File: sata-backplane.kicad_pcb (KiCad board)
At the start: 2 copper layers, 100 x 60 mm, 42 parts, among them J5 457180002, J6 G40H3132212HR

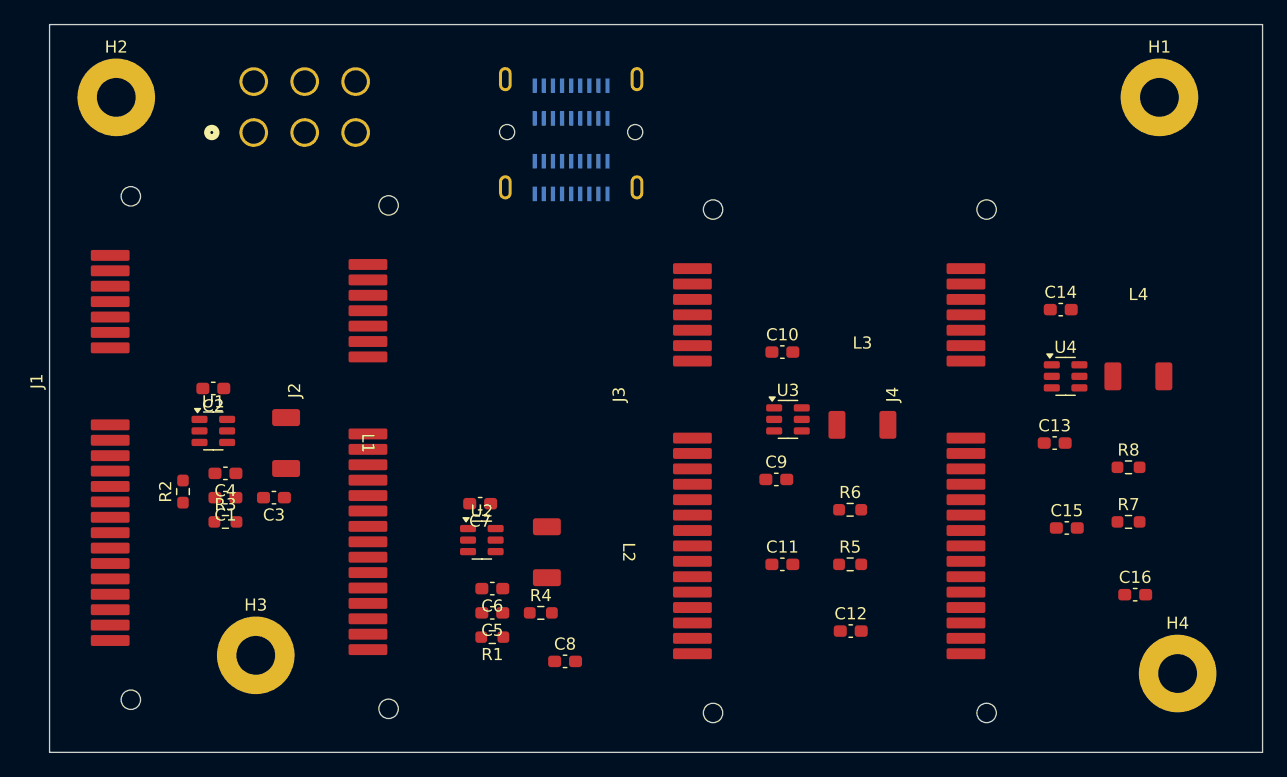
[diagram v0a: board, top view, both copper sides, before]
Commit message: Switch to two 3A converters from 4 2A
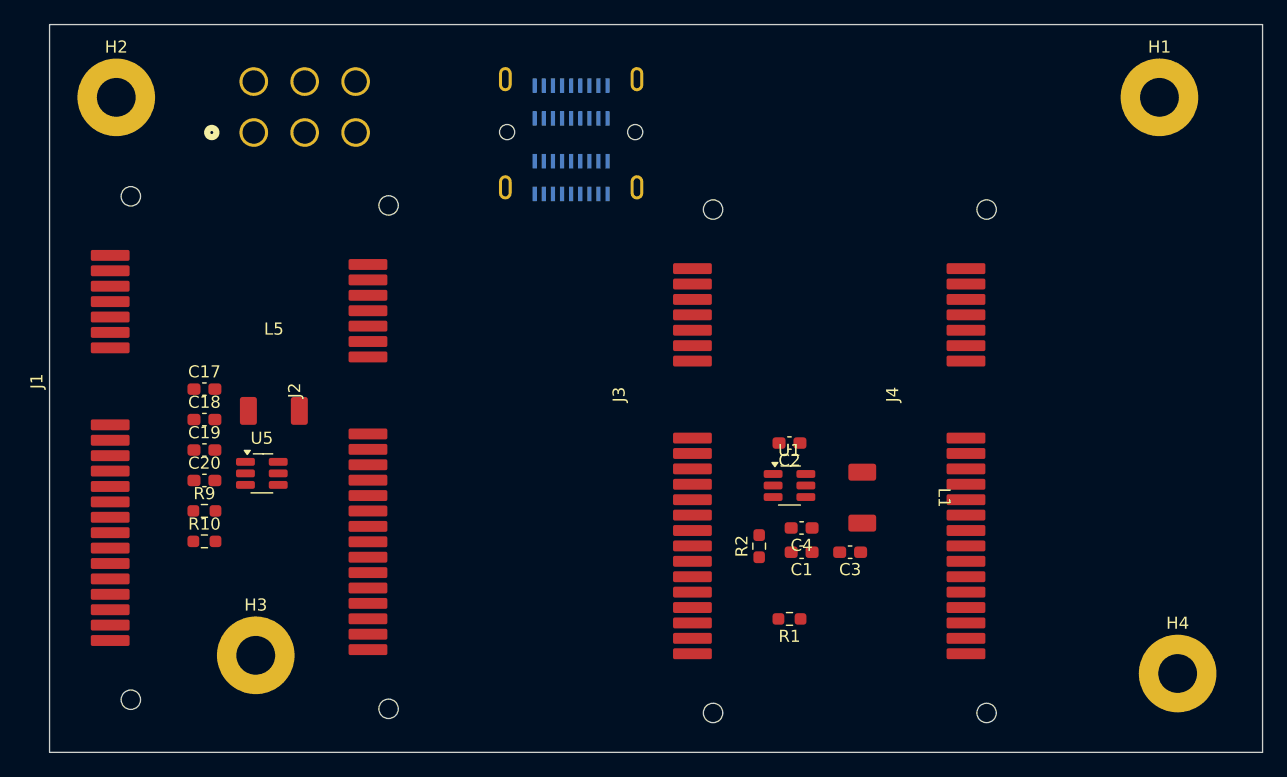
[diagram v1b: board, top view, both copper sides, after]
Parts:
- removed C10, C14, C6: 100nF, Capacitor_SMD:C_0603_1608Metric_Pad1.08x0.95mm_HandSolder
- removed C11, C15, C7: 22nF, Capacitor_SMD:C_0603_1608Metric_Pad1.08x0.95mm_HandSolder
- removed C12, C13, C16, C5, C8, C9: 22uF, Capacitor_SMD:C_0603_1608Metric_Pad1.08x0.95mm_HandSolder
- removed L2, L3, L4: 10uH, 00-Local:SL0420
- removed R3, R4, R6, R8: 82k, Resistor_SMD:R_0603_1608Metric_Pad0.98x0.95mm_HandSolder
- removed R5, R7: 11k, Resistor_SMD:R_0603_1608Metric_Pad0.98x0.95mm_HandSolder
- removed U2, U3, U4: ~, Package_TO_SOT_SMD:SOT-23-6
- added C17: 100nF, Capacitor_SMD:C_0603_1608Metric_Pad1.08x0.95mm_HandSolder, F.Cu at (150.3, 97.6)
- added C18: 22uF, Capacitor_SMD:C_0603_1608Metric_Pad1.08x0.95mm_HandSolder, F.Cu at (150.3, 100.1)
- added C19: 10uF, Capacitor_SMD:C_0603_1608Metric_Pad1.08x0.95mm_HandSolder, F.Cu at (150.3, 102.6)
- added C20: 100nF, Capacitor_SMD:C_0603_1608Metric_Pad1.08x0.95mm_HandSolder, F.Cu at (150.3, 105.1)
- added L5: 3.3uH 20mOhm, 00-Local:SL0420, F.Cu at (156.0, 99.3)
- added R10: 56.2k, Resistor_SMD:R_0603_1608Metric_Pad0.98x0.95mm_HandSolder, F.Cu at (150.3, 110.1)
- added R9: 10k, Resistor_SMD:R_0603_1608Metric_Pad0.98x0.95mm_HandSolder, F.Cu at (150.3, 107.6)
- added U5: TPS563201DDCR, Package_TO_SOT_SMD:SOT-23-6_Handsoldering, F.Cu at (155.0, 104.5)
- C1: value 22uF -> 10uF
- C2: value 22nF -> 100nF
- C3: value 22uF -> 100nF
- C4: value 100nF -> 22uF
- L1: value 10uH -> 3.3uH 20mOhm
- R1: value 11k -> 10k
- R2: value 11k -> 56.2k
- U1: value ~ -> TPS563201DDCR; footprint Package_TO_SOT_SMD:SOT-23-6 -> Package_TO_SOT_SMD:SOT-23-6_Handsoldering
- moved C1 47.7 mm to (199.5, 111.0)
- moved C2 47.7 mm to (198.5, 102.0)
- moved C3 47.7 mm to (203.5, 111.0)
- moved C4 47.7 mm to (199.5, 109.0)
- moved L1 47.7 mm to (204.5, 106.5)
- moved R2 47.7 mm to (196.0, 110.5)
- moved U1 47.7 mm to (198.5, 105.5)
- moved R1 24.5 mm to (198.5, 116.5)
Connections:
- C1 pad 1: +12V -> Net-(U1-EN)
- C2 pad 1: Net-(U1-SW) -> Net-(U1-EN)
- C2 pad 2: Net-(U1-BS) -> GND
- C3 pad 1: GND -> Net-(U1-SW)
- C3 pad 2: +5V_1 -> Net-(U1-VBST)
- C4 pad 1: +12V -> GND
- C4 pad 2: GND -> +5V_2
- J2 pad 14: +5V_2 -> +5V_1
- J2 pad 15: +5V_2 -> +5V_1
- J2 pad 16: +5V_2 -> +5V_1
- J3 pad 14: +5V_3 -> +5V_2
- J3 pad 15: +5V_3 -> +5V_2
- J3 pad 16: +5V_3 -> +5V_2
- J4 pad 14: +5V_4 -> +5V_2
- J4 pad 15: +5V_4 -> +5V_2
- J4 pad 16: +5V_4 -> +5V_2
- L1 pad 2: +5V_1 -> +5V_2
- R1 pad 1: Net-(U2-FB) -> Net-(U1-VFB)
- R2 pad 1: Net-(U1-FB) -> Net-(U1-VFB)
- R2 pad 2: GND -> +5V_2
- U1 pad 1: Net-(U1-BS) -> GND
- U1 pad 2: GND -> Net-(U1-SW)
- U1 pad 3: Net-(U1-FB) -> Net-(U1-EN)
- U1 pad 4: +12V -> Net-(U1-VFB)
- U1 pad 5: +12V -> Net-(U1-EN)
- U1 pad 6: Net-(U1-SW) -> Net-(U1-VBST)

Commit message: Rough layout
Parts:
- J1, J2, J3, J4: moved to B.Cu
- J5: moved to F.Cu
- J6: footprint G40H3132212HR:AMPHENOL_G40H3132212HR -> 00-Local:AMPHENOL_G40H3132212HR; moved to F.Cu
- moved J5 59.1 mm to (193.2, 120.9), turned to 0 degrees
- moved C2 28.2 mm to (224.5, 113.0), turned to -90 degrees
- moved U1 25.1 mm to (223.5, 108.0)
- moved C4 23.2 mm to (222.0, 103.5), turned to -90 degrees
- moved C1 22.6 mm to (222.0, 113.0), turned to -90 degrees
- moved C3 22.3 mm to (224.5, 103.5), turned to -90 degrees
- moved J4 21.4 mm to (234.0, 97.0)
- moved R1 21.3 mm to (219.5, 113.0), turned to -90 degrees
- moved R2 21.1 mm to (217.0, 113.0)
- moved C20 16.7 mm to (165.0, 113.0), turned to -90 degrees
- moved C19 16.1 mm to (162.5, 113.0), turned to -90 degrees
- moved C17 15.9 mm to (165.0, 103.5), turned to 90 degrees
- moved J3 14.7 mm to (204.5, 97.0)
- moved L1 13.0 mm to (217.5, 107.0), turned to 90 degrees
- moved C18 12.7 mm to (162.5, 103.5), turned to 90 degrees
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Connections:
- C1 pad 1: Net-(U1-EN) -> +12V
- C19 pad 1: Net-(U5-EN) -> +12V
- C2 pad 1: Net-(U1-EN) -> +12V
- C20 pad 1: Net-(U5-EN) -> +12V
- J5 pad 4: unconnected-(J5-Pad4) -> GND
- U1 pad 3: Net-(U1-EN) -> +12V
- U1 pad 5: Net-(U1-EN) -> +12V
- U5 pad 3: Net-(U5-EN) -> +12V
- U5 pad 5: Net-(U5-EN) -> +12V
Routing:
- net GND: vias 0 -> 10
- added copper zone on B.Cu, net +12V
- added copper zone on B.Cu, net +5V_1
- added copper zone on B.Cu, net +5V_2
- added copper zone on B.Cu, net GND
- added copper zone on F.Cu, net GND

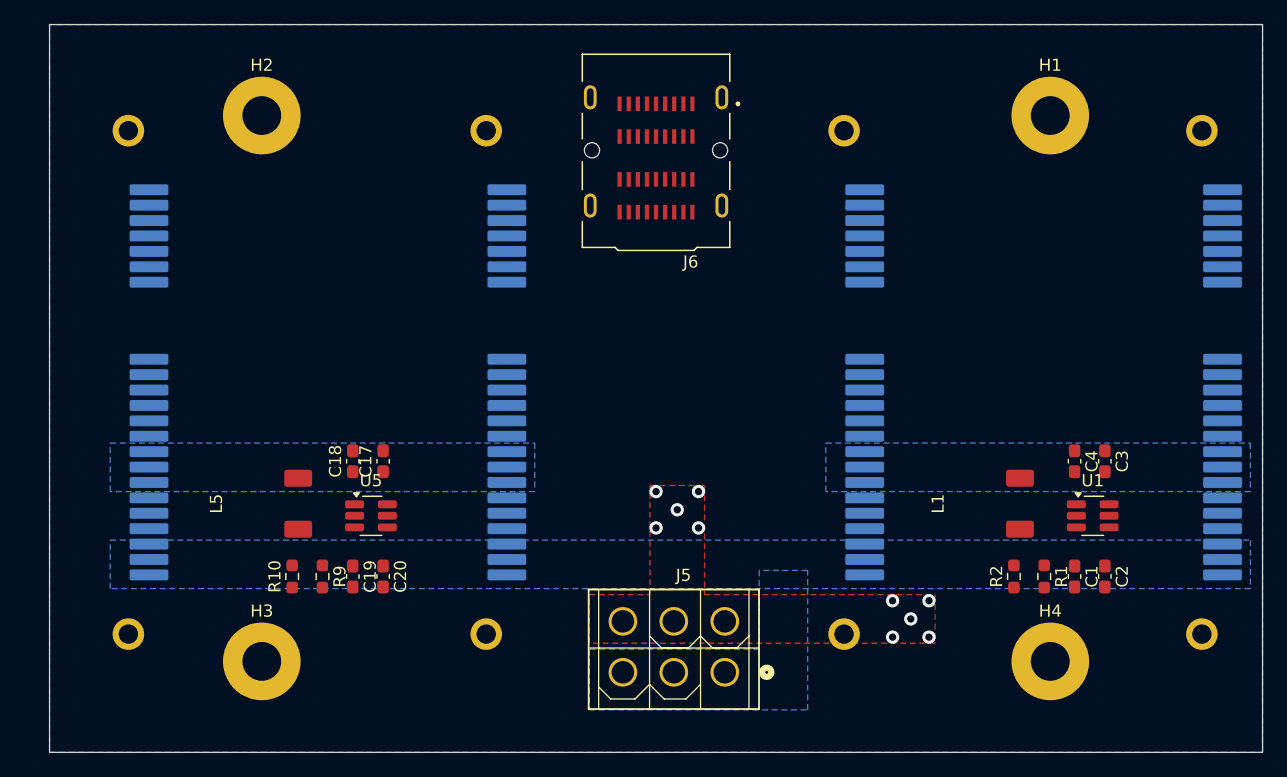
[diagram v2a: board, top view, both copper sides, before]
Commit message: Wire up power
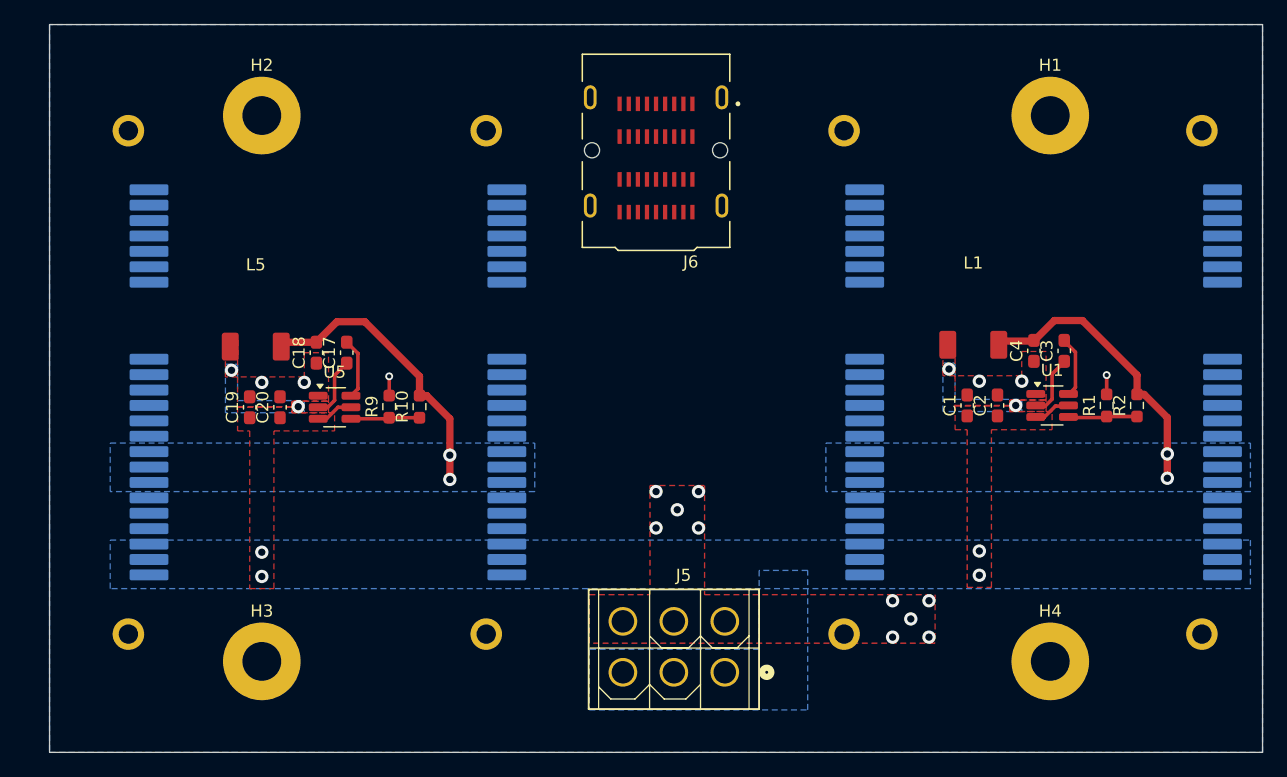
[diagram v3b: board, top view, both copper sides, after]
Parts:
- moved R10 17.5 mm to (168.0, 99.0)
- moved R2 17.4 mm to (227.2, 98.9)
- moved C1 16.6 mm to (213.2, 98.9), turned to 90 degrees
- moved C2 16.6 mm to (215.7, 98.9), turned to 90 degrees
- moved C19 16.3 mm to (154.0, 99.0), turned to 90 degrees
- moved C20 16.3 mm to (156.5, 99.0), turned to 90 degrees
- moved R9 15.0 mm to (165.5, 99.0), turned to 90 degrees
- moved R1 15.0 mm to (224.7, 98.9), turned to 90 degrees
- moved L1 13.7 mm to (213.7, 93.9), turned to 0 degrees
- moved L5 13.4 mm to (154.5, 94.0), turned to 0 degrees
- moved C3 9.70 mm to (221.2, 94.4), turned to 90 degrees
- moved C4 9.70 mm to (218.7, 94.4), turned to 90 degrees
- moved U1 9.70 mm to (220.2, 98.9)
- moved C17 9.44 mm to (162.0, 94.5)
- moved C18 9.44 mm to (159.5, 94.5)
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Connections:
- J1 pad 10: +3.3V -> unconnected-(J1-V33-Pad10)
- J1 pad 8: +3.3V -> unconnected-(J1-V33-Pad8)
- J1 pad 9: +3.3V -> unconnected-(J1-V33-Pad9)
- J2 pad 10: +3.3V -> unconnected-(J2-V33-Pad10)
- J2 pad 8: +3.3V -> unconnected-(J2-V33-Pad8)
- J2 pad 9: +3.3V -> unconnected-(J2-V33-Pad9)
- J3 pad 10: +3.3V -> unconnected-(J3-V33-Pad10)
- J3 pad 8: +3.3V -> unconnected-(J3-V33-Pad8)
- J3 pad 9: +3.3V -> unconnected-(J3-V33-Pad9)
- J4 pad 10: +3.3V -> unconnected-(J4-V33-Pad10)
- J4 pad 8: +3.3V -> unconnected-(J4-V33-Pad8)
- J4 pad 9: +3.3V -> unconnected-(J4-V33-Pad9)
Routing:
- net +5V_1: track 0.00 -> 24.0 mm, vias 0 -> 2
- net +5V_2: track 0.00 -> 24.0 mm, vias 0 -> 2
- net +12V: track 0.00 -> 6.19 mm, vias 0 -> 4
- net Net-(U5-VFB): track 0.00 -> 5.69 mm
- net Net-(U1-VFB): track 0.00 -> 5.69 mm
- net Net-(U5-SW): track 0.00 -> 5.14 mm, vias 0 -> 2
- net Net-(U1-SW): track 0.00 -> 5.14 mm, vias 0 -> 2
- net Net-(U1-VBST): track 0.00 -> 5.03 mm
- net Net-(U5-VBST): track 0.00 -> 5.03 mm
- net GND: track 0.00 -> 3.17 mm, vias 10 -> 16
- added copper zone on F.Cu, net +12V
- added copper zone on B.Cu, net Net-(U1-SW)
- added copper zone on F.Cu, net Net-(U1-SW)
- added copper zone on B.Cu, net Net-(U5-SW)
- added copper zone on F.Cu, net Net-(U5-SW)

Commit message: Routed
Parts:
- moved J6 1.00 mm to (188.5, 78.5), turned to 0 degrees
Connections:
- J6 pad A4: /S1_B- -> /S2_B+
- J6 pad A5: /S1_B+ -> /S2_B-
- J6 pad A7: /S3_B- -> /S4_B+
- J6 pad A8: /S3_B+ -> /S4_B-
- J6 pad B4: /S4_A+ -> /S1_B+
- J6 pad B5: /S4_A- -> /S1_B-
- J6 pad B7: /S4_B- -> /S3_B+
- J6 pad B8: /S4_B+ -> /S3_B-
- J6 pad C4: /S1_A+ -> /S2_A+
- J6 pad C5: /S1_A- -> /S2_A-
- J6 pad C7: /S3_A+ -> /S4_A+
- J6 pad C8: /S3_A- -> /S4_A-
- J6 pad D4: /S2_A+ -> /S1_A+
- J6 pad D5: /S2_A- -> /S1_A-
- J6 pad D7: /S2_B- -> /S3_A+
- J6 pad D8: /S2_B+ -> /S3_A-
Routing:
- net /S1_A-: track 0.00 -> 65.4 mm, vias 0 -> 1
- net /S1_A+: track 0.00 -> 65.3 mm, vias 0 -> 1
- net /S4_B+: track 0.00 -> 53.3 mm, vias 0 -> 1
- net /S4_B-: track 0.00 -> 53.2 mm, vias 0 -> 1
- net /S4_A+: track 0.00 -> 48.9 mm, vias 0 -> 1
- net /S4_A-: track 0.00 -> 48.8 mm, vias 0 -> 1
- net /S1_B-: track 0.00 -> 48.8 mm, vias 0 -> 1
- net /S1_B+: track 0.00 -> 48.8 mm, vias 0 -> 1
- net /S2_A-: track 0.00 -> 33.8 mm, vias 0 -> 1
- net /S2_A+: track 0.00 -> 33.7 mm, vias 0 -> 1
- net /S2_B-: track 0.00 -> 31.6 mm, vias 0 -> 1
- net /S2_B+: track 0.00 -> 31.5 mm, vias 0 -> 1
- net /S3_A+: track 0.00 -> 23.2 mm, vias 0 -> 1
- net /S3_A-: track 0.00 -> 23.2 mm, vias 0 -> 1
- net /S3_B+: track 0.00 -> 19.5 mm, vias 0 -> 1
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
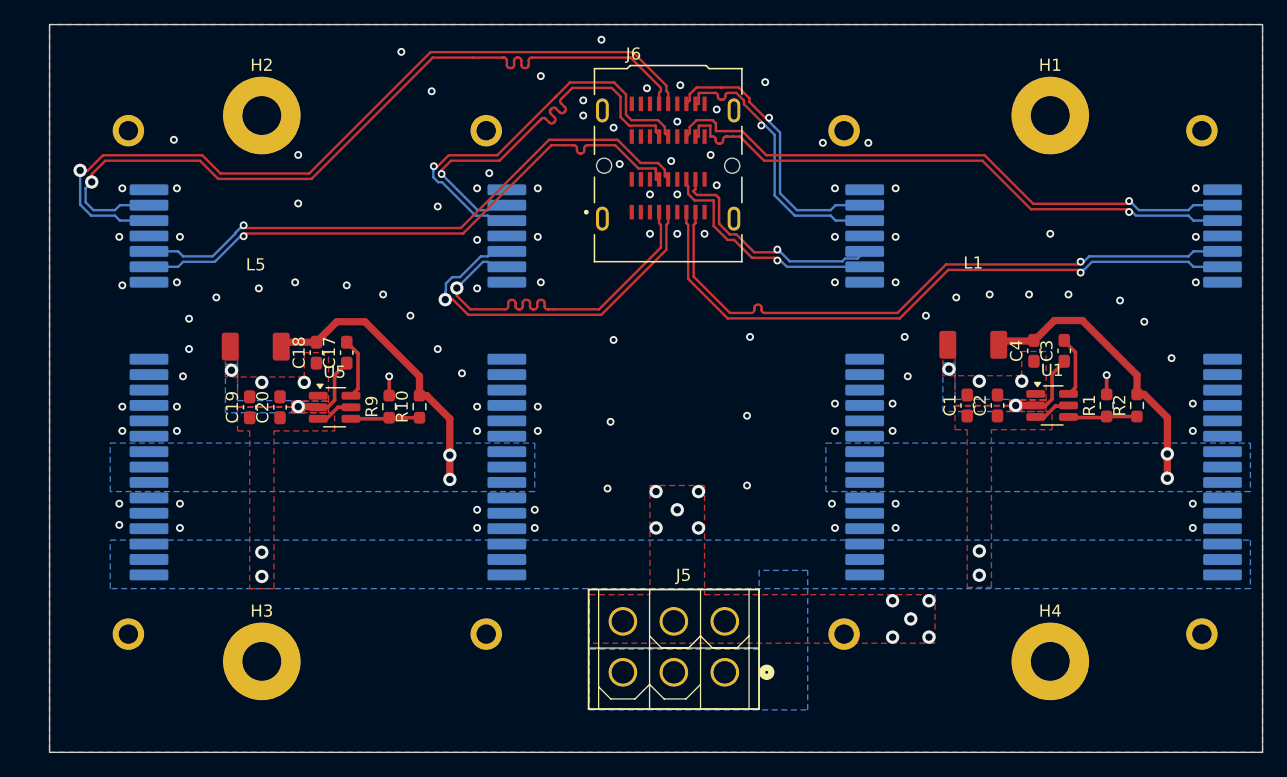
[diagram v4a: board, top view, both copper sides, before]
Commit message: Add Molex HD power connector
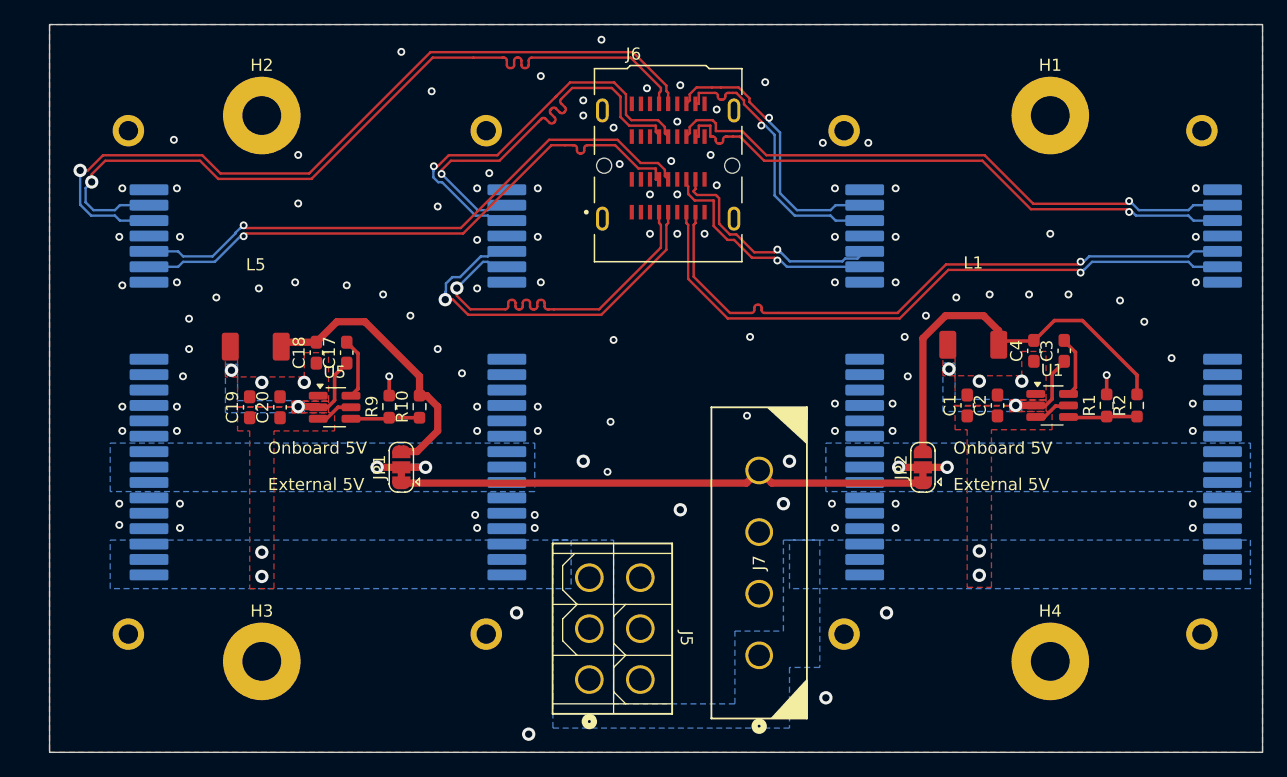
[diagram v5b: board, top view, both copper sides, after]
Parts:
- added J7: Conn_01x04, 00-Local:350211-1_TYC, F.Cu at (196.0, 119.5)
- added JP1: SolderJumper_3_Open, Jumper:SolderJumper-3_P1.3mm_Bridged12_RoundedPad1.0x1.5mm, F.Cu at (166.5, 104.0)
- added JP2: SolderJumper_3_Open, Jumper:SolderJumper-3_P1.3mm_Bridged12_RoundedPad1.0x1.5mm, F.Cu at (209.5, 104.0)
- moved J5 11.2 mm to (182.0, 121.5), turned to -90 degrees
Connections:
- C18 pad 2: +5V_1 -> /Converter1
- C4 pad 2: +5V_2 -> /Converter2
- L1 pad 2: +5V_2 -> /Converter2
- L5 pad 2: +5V_1 -> /Converter1
- R10 pad 2: +5V_1 -> /Converter1
- R2 pad 2: +5V_2 -> /Converter2
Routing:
- net +5V: track 0.00 -> 43.9 mm
- net /Converter2: track 0.00 -> 33.7 mm
- net /Converter1: track 0.00 -> 23.3 mm
- net +5V_2: track 24.0 -> 4.00 mm
- net +5V_1: track 24.0 -> 6.00 mm
- net GND: vias 121 -> 118
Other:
- board text added: "External 5V"
- board text added: "Onboard 5V"
